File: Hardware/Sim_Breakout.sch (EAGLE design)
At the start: 7 parts, among them U2 SIMHOLDER

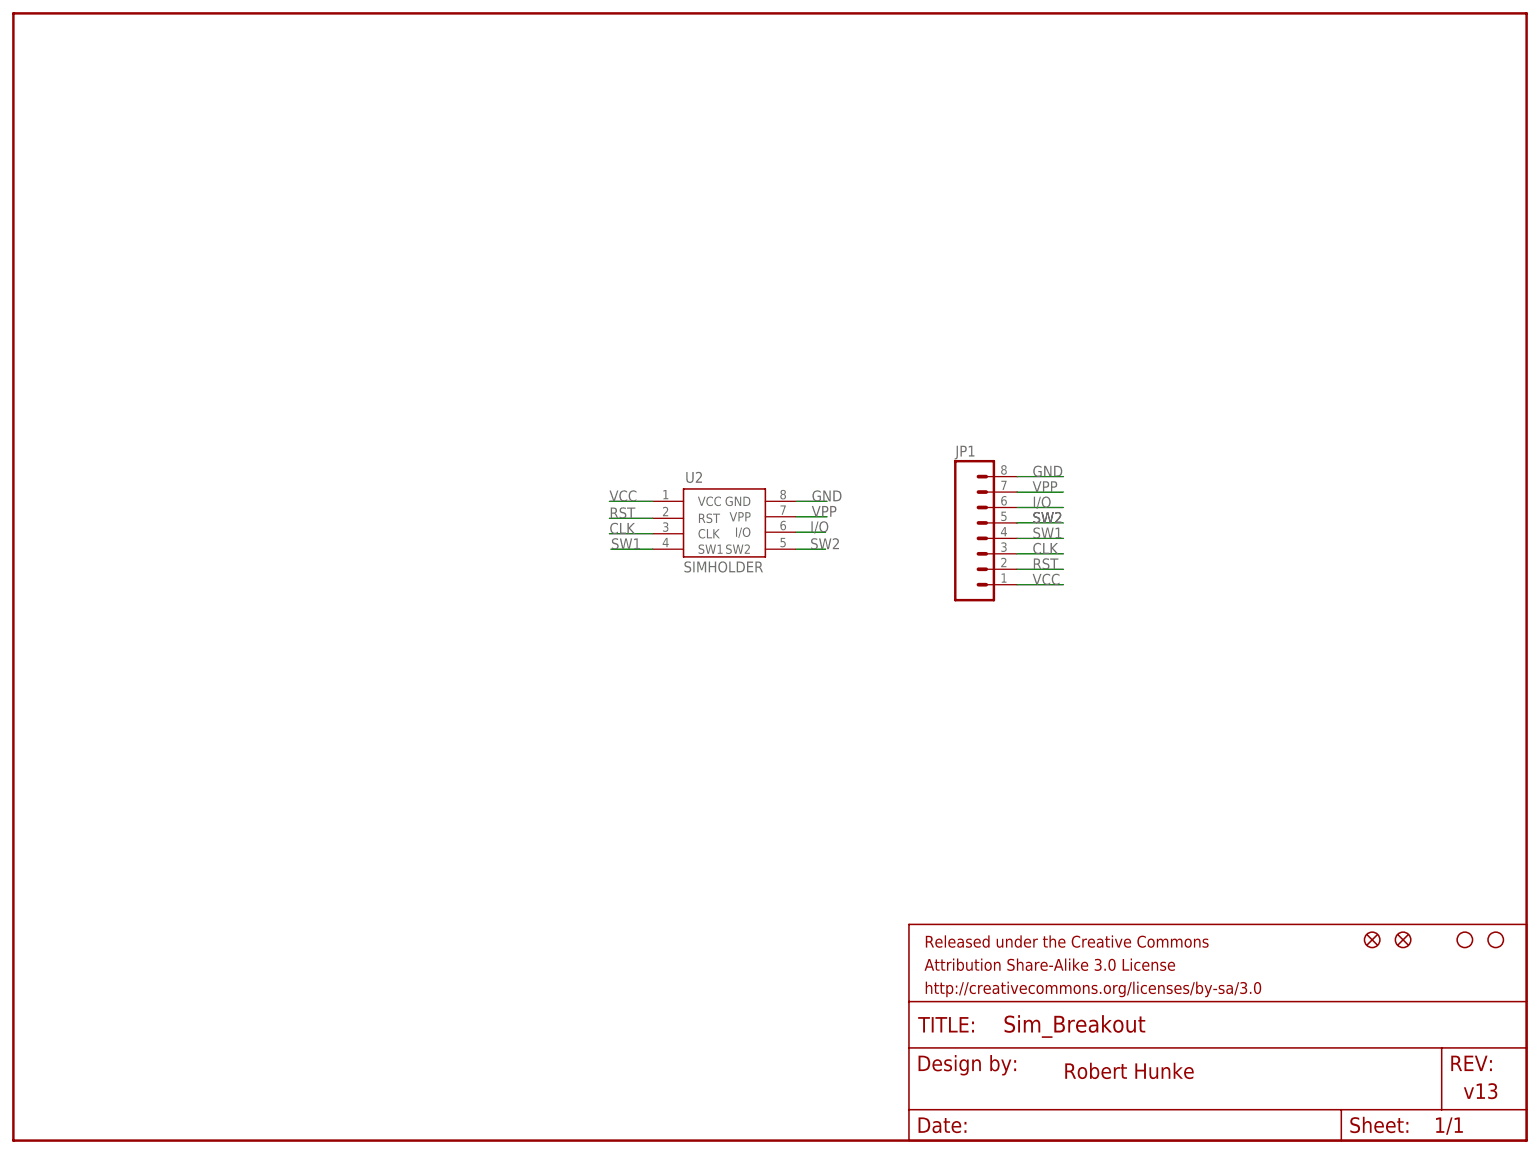
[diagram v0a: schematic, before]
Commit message: Aesthetic changes
1. Updated net labels to flags.
2.) Added OSHW logo to bottom silk.
3.) Added SFE logo to bottom silk.
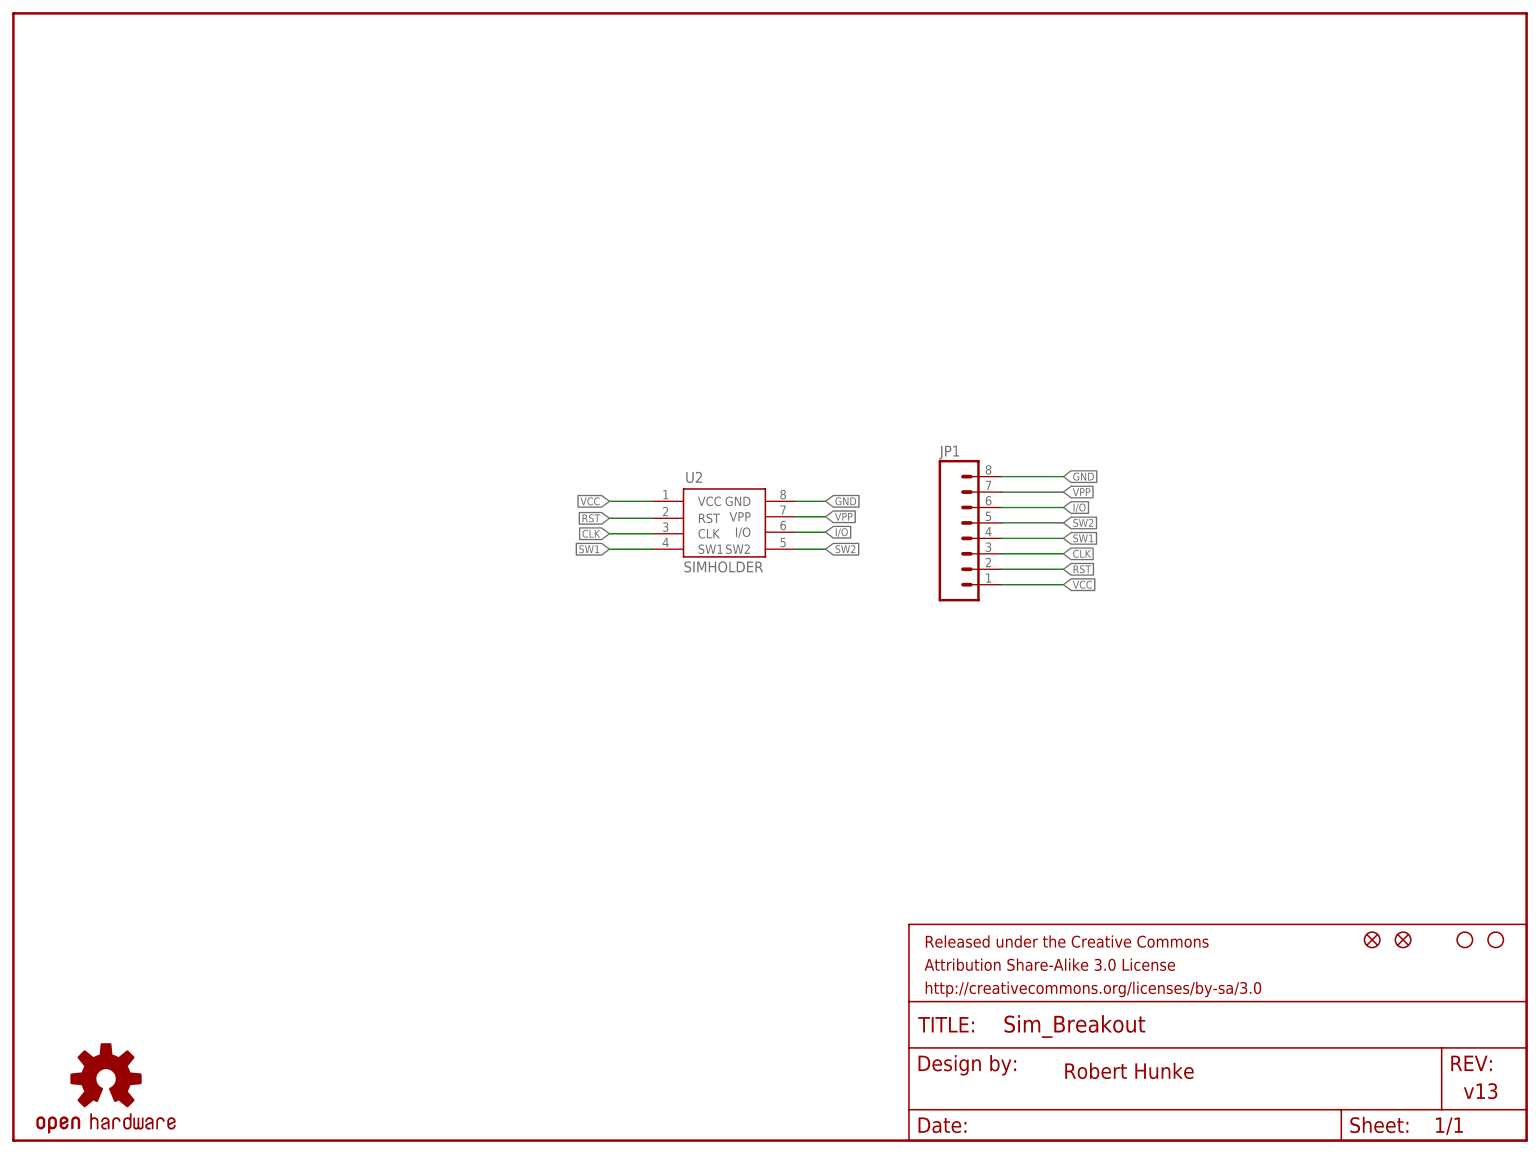
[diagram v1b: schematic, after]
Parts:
- added LOGO1: OSHW-LOGOS, SparkFun-Aesthetics:OSHW-LOGOS
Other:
- moved on the sheet: JP1
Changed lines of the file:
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@@
 <part name="FID1" library="SparkFun-Aesthetics" deviceset="FIDUCIAL" device="UFIDUCIAL"/>
 <part name="FID2" library="SparkFun-Aesthetics" deviceset="FIDUCIAL" device="UFIDUCIAL"/>
+<part name="LOGO1" library="SparkFun-Aesthetics" deviceset="OSHW-LOGO" device="S"/>
 </parts>
 <sheets>
@@
 </plain>
 <instances>
-<instance part="JP1" gate="G$1" x="157.48" y="99.06"/>
+<instance part="JP1" gate="G$1" x="154.94" y="99.06"/>
 <instance part="U2" gate="G$1" x="114.3" y="101.6"/>
 <instance part="STANDOFF1" gate="G$1" x="236.22" y="33.02"/>
@@
 <instance part="FID1" gate="G$1" x="220.98" y="33.02"/>
 <instance part="FID2" gate="G$1" x="226.06" y="33.02"/>
+<instance part="LOGO1" gate="G$1" x="12.7" y="10.16"/>
 </instances>
 <busses>
@@
 <net name="VCC" class="0">
 <segment>
-<wire x1="162.56" y1="91.44" x2="170.18" y2="91.44" width="0.1524" layer="91"/>
-<label x="165.1" y="91.44" size="1.778" layer="95"/>
+<wire x1="160.02" y1="91.44" x2="170.18" y2="91.44" width="0.1524" layer="91"/>
 <pinref part="JP1" gate="G$1" pin="1"/>
+<label x="170.18" y="91.44" size="1.27" layer="95" xref="yes"/>
 </segment>
 <segment>
 <wire x1="102.616" y1="105.156" x2="95.504" y2="105.156" width="0.1524" layer="91"/>
-<label x="95.504" y="105.156" size="1.778" layer="95"/>
 <pinref part="U2" gate="G$1" pin="VCC"/>
+<label x="95.504" y="105.156" size="1.27" layer="95" rot="R180" xref="yes"/>
 </segment>
 </net>
@@
 <segment>
 <wire x1="102.616" y1="102.362" x2="95.504" y2="102.362" width="0.1524" layer="91"/>
-<label x="95.504" y="102.362" size="1.778" layer="95"/>
 <pinref part="U2" gate="G$1" pin="RST"/>
+<label x="95.504" y="102.362" size="1.27" layer="95" rot="R180" xref="yes"/>
 </segment>
 <segment>
-<wire x1="162.56" y1="93.98" x2="170.18" y2="93.98" width="0.1524" layer="91"/>
-<label x="165.1" y="93.98" size="1.778" layer="95"/>
+<wire x1="160.02" y1="93.98" x2="170.18" y2="93.98" width="0.1524" layer="91"/>
 <pinref part="JP1" gate="G$1" pin="2"/>
+<label x="170.18" y="93.98" size="1.27" layer="95" xref="yes"/>
 </segment>
 </net>
@@
 <segment>
 <wire x1="102.616" y1="99.822" x2="95.504" y2="99.822" width="0.1524" layer="91"/>
-<label x="95.504" y="99.822" size="1.778" layer="95"/>
 <pinref part="U2" gate="G$1" pin="CLK"/>
+<label x="95.504" y="99.822" size="1.27" layer="95" rot="R180" xref="yes"/>
 </segment>
 <segment>
-<wire x1="162.56" y1="96.52" x2="170.18" y2="96.52" width="0.1524" layer="91"/>
-<label x="165.1" y="96.52" size="1.778" layer="95"/>
+<wire x1="160.02" y1="96.52" x2="170.18" y2="96.52" width="0.1524" layer="91"/>
 <pinref part="JP1" gate="G$1" pin="3"/>
+<label x="170.18" y="96.52" size="1.27" layer="95" xref="yes"/>
 </segment>
 </net>
@@
 <segment>
 <wire x1="126.238" y1="100.076" x2="131.064" y2="100.076" width="0.1524" layer="91"/>
-<label x="128.524" y="100.076" size="1.778" layer="95"/>
 <pinref part="U2" gate="G$1" pin="I/O"/>
+<label x="131.064" y="100.076" size="1.27" layer="95" xref="yes"/>
 </segment>
 <segment>
-<wire x1="162.56" y1="104.14" x2="170.18" y2="104.14" width="0.1524" layer="91"/>
-<label x="165.1" y="104.14" size="1.778" layer="95"/>
+<wire x1="160.02" y1="104.14" x2="170.18" y2="104.14" width="0.1524" layer="91"/>
 <pinref part="JP1" gate="G$1" pin="6"/>
+<label x="170.18" y="104.14" size="1.27" layer="95" xref="yes"/>
 </segment>
 </net>
 <net name="VPP" class="0">
 <segment>
-<wire x1="126.238" y1="102.616" x2="131.318" y2="102.616" width="0.1524" layer="91"/>
-<label x="128.778" y="102.616" size="1.778" layer="95"/>
+<wire x1="126.238" y1="102.616" x2="131.064" y2="102.616" width="0.1524" layer="91"/>
 <pinref part="U2" gate="G$1" pin="VPP"/>
+<label x="131.064" y="102.616" size="1.27" layer="95" xref="yes"/>
 </segment>
 <segment>
-<wire x1="162.56" y1="106.68" x2="170.18" y2="106.68" width="0.1524" layer="91"/>
-<label x="165.1" y="106.68" size="1.778" layer="95"/>
+<wire x1="160.02" y1="106.68" x2="170.18" y2="106.68" width="0.1524" layer="91"/>
 <pinref part="JP1" gate="G$1" pin="7"/>
+<label x="170.18" y="106.68" size="1.27" layer="95" xref="yes"/>
 </segment>
 </net>
 <net name="GND" class="0">
 <segment>
-<wire x1="126.238" y1="105.156" x2="131.318" y2="105.156" width="0.1524" layer="91"/>
-<label x="128.778" y="105.156" size="1.778" layer="95"/>
+<wire x1="126.238" y1="105.156" x2="131.064" y2="105.156" width="0.1524" layer="91"/>
 <pinref part="U2" gate="G$1" pin="GND"/>
+<label x="131.064" y="105.156" size="1.27" layer="95" xref="yes"/>
 </segment>
 <segment>
-<wire x1="162.56" y1="109.22" x2="170.18" y2="109.22" width="0.1524" layer="91"/>
-<label x="165.1" y="109.22" size="1.778" layer="95"/>
+<wire x1="160.02" y1="109.22" x2="170.18" y2="109.22" width="0.1524" layer="91"/>
 <pinref part="JP1" gate="G$1" pin="8"/>
+<label x="170.18" y="109.22" size="1.27" layer="95" xref="yes"/>
 </segment>
 </net>
 <net name="SW1" class="0">
 <segment>
-<wire x1="102.616" y1="97.282" x2="95.758" y2="97.282" width="0.1524" layer="91"/>
-<label x="95.758" y="97.282" size="1.778" layer="95"/>
+<wire x1="102.616" y1="97.282" x2="95.504" y2="97.282" width="0.1524" layer="91"/>
 <pinref part="U2" gate="G$1" pin="SW1"/>
+<label x="95.504" y="97.282" size="1.27" layer="95" rot="R180" xref="yes"/>
 </segment>
 <segment>
-<wire x1="162.56" y1="99.06" x2="170.18" y2="99.06" width="0.1524" layer="91"/>
-<label x="165.1" y="99.06" size="1.778" layer="95"/>
+<wire x1="160.02" y1="99.06" x2="170.18" y2="99.06" width="0.1524" layer="91"/>
 <pinref part="JP1" gate="G$1" pin="4"/>
+<label x="170.18" y="99.06" size="1.27" layer="95" xref="yes"/>
 </segment>
 </net>
 <net name="SW2" class="0">
 <segment>
-<wire x1="162.56" y1="101.6" x2="170.18" y2="101.6" width="0.1524" layer="91"/>
-<label x="165.1" y="101.6" size="1.778" layer="95"/>
-<label x="165.1" y="101.6" size="1.778" layer="95"/>
+<wire x1="160.02" y1="101.6" x2="170.18" y2="101.6" width="0.1524" layer="91"/>
 <pinref part="JP1" gate="G$1" pin="5"/>
+<label x="170.18" y="101.6" size="1.27" layer="95" xref="yes"/>
 </segment>
 <segment>
 <wire x1="126.238" y1="97.282" x2="131.064" y2="97.282" width="0.1524" layer="91"/>
-<label x="128.524" y="97.282" size="1.778" layer="95"/>
 <pinref part="U2" gate="G$1" pin="SW2"/>
+<label x="131.064" y="97.282" size="1.27" layer="95" xref="yes"/>
 </segment>
 </net>
